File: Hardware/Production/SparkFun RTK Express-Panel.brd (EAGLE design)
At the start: 219.3 x 141.9 mm, 501 parts, among them J13 Internal, J16 External, J17 Qwiic Right Angle, J19 MICRO-SD-PUSH-PUSH-EXT-PIN, J21 USB Female Type C Connector, J24 USB Female Type C Connector, J3 USB Female Type C Connector, J32 Qwiic Right Angle, J33 Internal, J38 MICRO-SD-PUSH-PUSH-EXT-PIN, J39 External, J4 External, J40 USB Female Type C Connector, J43 USB Female Type C Connector, J5 USB Female Type C Connector, J51 Qwiic Right Angle, J52 Internal, J57 MICRO-SD-PUSH-PUSH-EXT-PIN, Q1 SIL2308-TP, Q2 MBT3904DW1T1, Q3 MBT3904DW1T1, Q4 SIL2308-TP, Q5 MBT3904DW1T1, Q6 SIL2308-TP, U1 74HC4052D, U10 MCP73833, U11 CH340C, U12 MAX17048, U13 LIS2DH12, U14 STLQ015-3.3V, U15 MCP73833, U16 74HC4052D, U17 LIS2DH12, U18 ESP-WROOM-3232D, U19 AP2112K-3.3, U2 AP2112K-3.3, U20 U-BLOX_ZED-F9P, U21 CH340C, U22 MAX17048, U23 STLQ015-3.3V, U24 MCP73833, U25 74HC4052D, U26 LIS2DH12, U27 ESP-WROOM-3232D, U3 U-BLOX_ZED-F9P, U4 STLQ015-3.3V, U5 ESP-WROOM-3232D, U6 CH340C, U7 MAX17048, U8 AP2112K-3.3, U9 U-BLOX_ZED-F9P

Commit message: LIF overlay connector, accel plane removal, full ESP32 FP.
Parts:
- removed J55: (no value), SparkFun-Connectors:1X01_NO_SILK
- removed J56: (no value), SparkFun-Connectors:FPC_12_0.5MM
- removed J57: MICRO-SD-PUSH-PUSH-EXT-PIN, SparkFun-Connectors:MICROSD-EXTERNALPIN
- added JP12: FIDUCIALUFIDUCIAL, SparkFun-Aesthetics:FIDUCIAL-MICRO
- added JP13: JUMPER-SMT_2_NO_SILK, SparkFun-Jumpers:SMT-JUMPER_2_NO_SILK
- added JP14: CONN_06, 1mm Pitch Connector:FPC_6_1MM-LIF
- J20: value (none) -> USB Female Type C Connector; device SparkFun-Connectors:FPC_12_0.5MM -> SparkFun-Connectors:USB-C-16P_4LAYER-PADS
- J21: value USB Female Type C Connector -> (none); device SparkFun-Connectors:USB-C-16P_4LAYER-PADS -> SparkFun-Connectors:JST-2-SMD
- J22: device SparkFun-Connectors:JST-2-SMD -> SparkFun-Connectors:1X02_NO_SILK
- J23: value (none) -> USB Female Type C Connector; device SparkFun-Connectors:1X02_NO_SILK -> SparkFun-Connectors:USB-C-16P_4LAYER-PADS
- J24, J43: value USB Female Type C Connector -> (none); device SparkFun-Connectors:USB-C-16P_4LAYER-PADS -> SparkFun-Connectors:JST-4-SMD-1.25MM-LOCKING
- J26, J44, J45: device SparkFun-Connectors:JST-4-SMD-1.25MM-LOCKING -> SparkFun-Connectors:1X04_NO_SILK
- J29, J47, J48: device SparkFun-Connectors:1X04_NO_SILK -> SparkFun-Connectors:1X02_NO_SILK
- J31, J49: value (none) -> Qwiic Right Angle; device SparkFun-Connectors:1X02_NO_SILK -> SparkFun-Connectors:1X04_NO_SILK
- J32: value Qwiic Right Angle -> Internal; device SparkFun-Connectors:1X04_NO_SILK -> SparkFun-Connectors:JST04_1MM_RA
- J33: value Internal -> (none); device SparkFun-Connectors:JST04_1MM_RA -> SparkFun-Connectors:1X05_NO_SILK
- J34: device SparkFun-Connectors:1X05_NO_SILK -> SparkFun-Connectors:1X04_NO_SILK
- J35: device SparkFun-Connectors:1X04_NO_SILK -> SparkFun-Connectors:1X01_NO_SILK
- J36: value (none) -> MICRO-SD-PUSH-PUSH-EXT-PIN; device SparkFun-Connectors:1X01_NO_SILK -> SparkFun-Connectors:MICROSD-EXTERNALPIN
- J37: value (none) -> External; device SparkFun-Connectors:FPC_12_0.5MM -> SparkFun-Connectors:JST04_1MM_RA
- J38: value MICRO-SD-PUSH-PUSH-EXT-PIN -> USB Female Type C Connector; device SparkFun-Connectors:MICROSD-EXTERNALPIN -> SparkFun-Connectors:USB-C-16P_4LAYER-PADS
- J39: value External -> (none); device SparkFun-Connectors:JST04_1MM_RA -> SparkFun-Connectors:JST-2-SMD
- J40: value USB Female Type C Connector -> (none); device SparkFun-Connectors:USB-C-16P_4LAYER-PADS -> SparkFun-Connectors:1X02_NO_SILK
- J41: value (none) -> USB Female Type C Connector; device SparkFun-Connectors:JST-2-SMD -> SparkFun-Connectors:USB-C-16P_4LAYER-PADS
- J42: device SparkFun-Connectors:1X02_NO_SILK -> SparkFun-Connectors:JST-4-SMD-1.25MM-LOCKING
- J50: value (none) -> Internal; device SparkFun-Connectors:1X02_NO_SILK -> SparkFun-Connectors:JST04_1MM_RA
- J51: value Qwiic Right Angle -> (none); device SparkFun-Connectors:1X04_NO_SILK -> SparkFun-Connectors:1X05_NO_SILK
- J52: value Internal -> (none); device SparkFun-Connectors:JST04_1MM_RA -> SparkFun-Connectors:1X04_NO_SILK
- J53: device SparkFun-Connectors:1X05_NO_SILK -> SparkFun-Connectors:1X01_NO_SILK
- J54: value (none) -> MICRO-SD-PUSH-PUSH-EXT-PIN; device SparkFun-Connectors:1X04_NO_SILK -> SparkFun-Connectors:MICROSD-EXTERNALPIN
- JP11, JP6: value JUMPER-SMT_2_NO_SILK -> FIDUCIALUFIDUCIAL; device SparkFun-Jumpers:SMT-JUMPER_2_NO_SILK -> SparkFun-Aesthetics:FIDUCIAL-MICRO
- JP2, JP8: value FIDUCIALUFIDUCIAL -> CONN_06; device SparkFun-Aesthetics:FIDUCIAL-MICRO -> 1mm Pitch Connector:FPC_6_1MM-LIF
- JP7: value FIDUCIALUFIDUCIAL -> JUMPER-SMT_2_NO_SILK; device SparkFun-Aesthetics:FIDUCIAL-MICRO -> SparkFun-Jumpers:SMT-JUMPER_2_NO_SILK
- R10: value 10 -> 27
- R11: value 100k -> 10
- R12: value 5.1k -> 100k
- R18: value 10k -> 5.1k; device SparkFun-Resistors:0603@1 -> SparkFun-Resistors:0603
- R45, R73: value 10k -> 1k; device SparkFun-Resistors:0603@1 -> SparkFun-Resistors:0603
- R46, R74: value 1k -> 33; device SparkFun-Resistors:0603 -> SparkFun-Resistors:1206_RA
- R50, R78: value 33 -> 100k; device SparkFun-Resistors:1206_RA -> SparkFun-Resistors:0603
- R51, R79: value 100k -> 300k
- R52, R80: value 300k -> 100k
- R53, R81: value 100k -> 10k
- R54, R82: value 10k -> 3.3k
- R55, R83: value 3.3k -> 10k
- R6: value 27 -> 10k
- moved JP7 137.9 mm to (73.9, 58.3), turned to 180 degrees
- moved R18 136.3 mm to (106.9, 10.3), flipped to the top, turned to 180 degrees
- moved JP2 125.5 mm to (51.2, 100.3), turned to 180 degrees
- moved JP3 116.5 mm to (132.1, 4.28)
- moved JP4 116.5 mm to (73.8, 105.2), flipped to the top
- moved JP5 116.5 mm to (132.1, 4.28)
- moved R6 109.3 mm to (11.2, 107.3), flipped to the bottom, turned to 0 degrees
- moved J37 105.1 mm to (171.6, 4.74), flipped to the bottom, turned to 0 degrees
- moved J42 104.0 mm to (148.7, 1.19), flipped to the top, turned to 0 degrees
- moved J20 103.9 mm to (102.9, 6.14), turned to 0 degrees
- moved J41 102.1 mm to (183.0, 6.14), turned to 0 degrees
- moved J23 101.4 mm to (114.3, 6.14), flipped to the top, turned to 0 degrees
- moved J39 100.5 mm to (151.6, 103.3), flipped to the top, turned to 90 degrees
- moved J40 99.3 mm to (158.9, 104.7), flipped to the bottom, turned to 270 degrees
- moved J21 99.2 mm to (82.9, 103.3), turned to 90 degrees
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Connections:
- net 3.3V1: now also J25.1, J27.4, J31.2, J36.4, R12.2, R55.2; no longer J26.1, J29.4, J33.2, J38.4, R11.2, R56.2
- net 3.3V2: now also J37.2, J43.1, J45.4, J46.4, J49.2, J50.2, J54.4, R83.2; no longer J39.2, J45.1, J47.4, J48.4, J51.2, J52.2, J57.4, R84.2
- net ANT_VCC1: now also R11.1; no longer R10.1
- net CC10: now also J38.B5; no longer J40.B5
- net CC11: now also J41.B5; no longer J43.B5
- net CC12: now also J41.A5; no longer J43.A5
- net CC5: now also J20.A5; no longer J21.A5
- net CC6: now also J20.B5, R18.2; no longer J21.B5, R12.2
- net CC7: now also J23.B5; no longer J24.B5
- net CC8: now also J23.A5; no longer J24.A5
- net CC9: now also J38.A5; no longer J40.A5
- net CHG_LED_RES: now also JP2.2; no longer J20.3, J20.4
- net CHG_LED_RES1: now also J34.2, JP8.2; no longer J35.2, J37.3, J37.4
- net CHG_LED_RES2: now also J52.2, JP14.2; no longer J54.2, J56.3, J56.4
- net CHG_THERM1: now also R6.2; no longer R18.2
- net CHG_THERM2: now also R56.2; no longer R45.2
- net CHG_THERM3: now also R84.2; no longer R73.2
- net D+2: now also R8.1; no longer R6.1
- net D-2: now also R10.1; no longer R8.1
- net ESP32_EN1: now also J30.1; no longer J31.1
- net ESP32_EN2: now also J48.1; no longer J50.1
- net ESP_13/POWER_CTRL1: now also R50.1, R51.2; no longer R51.1, R52.2
- net ESP_13/POWER_CTRL2: now also R78.1, R79.2; no longer R79.1, R80.2
- net ESP_14/SETUP_BUTTON: now also JP2.4; no longer J20.7, J20.8
- net ESP_14/SETUP_BUTTON1: now also J34.3, JP8.4; no longer J35.3, J37.7, J37.8
- net ESP_14/SETUP_BUTTON2: now also J52.3, JP14.4; no longer J54.3, J56.7, J56.8
- net ESP_18/SCK1: now also J36.5; no longer J38.5
- net ESP_18/SCK2: now also J54.5; no longer J57.5
- net ESP_19/CIPO1: now also J36.7; no longer J38.7
- net ESP_19/CIPO2: now also J54.7; no longer J57.7
- net ESP_21/SDA1: now also J31.3, R47.P7; no longer J33.3, R48.P7
- net ESP_21/SDA2: now also J37.3, J49.3, J50.3, R75.P7; no longer J39.3, J51.3, J52.3, R76.P7
- net ESP_22/SCL1: now also J31.4, R47.P8; no longer J33.4, R48.P8
- net ESP_22/SCL2: now also J37.4, J49.4, J50.4, R75.P8; no longer J39.4, J51.4, J52.4, R76.P8
- net ESP_23/COPI1: now also J36.3; no longer J38.3
- net ESP_23/COPI2: now also J54.3; no longer J57.3
- net ESP_25/SD_!CS!1: now also J36.2; no longer J38.2
- net ESP_25/SD_!CS!2: now also J54.2; no longer J57.2
- net ESP_26/ZED_TX_READY_LV1: now also R48.P4; no longer R49.P4
- net ESP_26/ZED_TX_READY_LV2: now also R76.P4; no longer R77.P4
- net ESP_27/FAST_OFF1: now also R51.1; no longer R52.1
- net ESP_27/FAST_OFF2: now also R79.1; no longer R80.1
- net ESP_4/ACCEL_INT1: now also J35.1, JP7.1; no longer J36.1, JP6.1
- net ESP_4/ACCEL_INT2: now also J53.1, JP13.1; no longer J55.1, JP11.1
- net ESP_D1+1: now also J23.A6, J23.B6; no longer J24.A6, J24.B6
- net ESP_D1+2: now also J41.A6, J41.B6; no longer J43.A6, J43.B6
- net ESP_D1-1: now also J23.A7, J23.B7; no longer J24.A7, J24.B7
- net ESP_D1-2: now also J41.A7, J41.B7; no longer J43.A7, J43.B7
- net ESP_I16/ZED-TXO2: now also J29.1, R47.P5; no longer J30.1, R48.P5
- net ESP_I16/ZED-TXO3: now also J47.1, R75.P5; no longer J49.1, R76.P5
- net ESP_I34/ZED_TX_READY1: now also J33.1, R48.P5; no longer J34.1, R49.P5
- net ESP_I34/ZED_TX_READY2: now also J51.1, R76.P5; no longer J53.1, R77.P5
- net ESP_I35/DEVICE_SENSE1: now also R54.2, R55.1; no longer R55.2, R56.1
- net ESP_I35/DEVICE_SENSE2: now also R82.2, R83.1; no longer R83.2, R84.1
- net ESP_O17/ZED-RXI2: now also J29.2, R45.2, R47.P6; no longer J30.2, R46.2, R48.P6
- net ESP_O17/ZED-RXI3: now also J47.2, R73.2, R75.P6; no longer J49.2, R74.2, R76.P6
- net EXTERNAL_DATA_IN1: now also J25.3, J27.2; no longer J26.3, J28.2
- net EXTERNAL_DATA_IN2: now also J43.3, J45.2; no longer J45.3, J47.2
- net EXTERNAL_DATA_OUT1: now also J25.2, J27.3; no longer J26.2, J28.3
- net EXTERNAL_DATA_OUT2: now also J43.2, J45.3; no longer J45.2, J47.3
- net EXTINT_LV1: now also R49.P2; no longer R50.P2
- net EXTINT_LV2: now also R77.P2; no longer R78.P2
- net FENCE_LV1: now also R46.P4; no longer R47.P4
- net FENCE_LV2: now also R74.P4; no longer R75.P4
- net GND: now also JP2.6, R6.1; no longer J20.11, J20.12, R18.1
- net GND1: now also J20.GND, J20.GND2, J20.SHLD1, J20.SHLD2, J20.SHLD3, J20.SHLD4, J21.1, J22.2, J23.GND, J23.GND2, J23.SHLD1, J23.SHLD2, J23.SHLD3, J23.SHLD4, J24.4, J26.1, J30.2, J31.1, J34.1, J36.10, J36.11, J36.12, J36.13, J36.6, J36.9, JP8.6, R18.1, R54.1, R56.1; no longer J21.GND, J21.GND2, J21.SHLD1, J21.SHLD2, J21.SHLD3, J21.SHLD4, J22.1, J23.2, J24.GND, J24.GND2, J24.SHLD1, J24.SHLD2, J24.SHLD3, J24.SHLD4, J26.4, J29.1, J31.2, J33.1, J35.1, J37.11, J37.12, J38.10, J38.11, J38.12, J38.13, J38.6, J38.9, R11.1, R45.1, R55.1
- net GND2: now also J37.1, J38.GND, J38.GND2, J38.SHLD1, J38.SHLD2, J38.SHLD3, J38.SHLD4, J40.2, J41.GND, J41.GND2, J41.SHLD1, J41.SHLD2, J41.SHLD3, J41.SHLD4, J42.4, J43.4, J44.1, J45.1, J48.2, J49.1, J50.1, J54.10, J54.11, J54.12, J54.13, J54.6, J54.9, JP14.6, R82.1, R84.1; no longer J40.GND, J40.GND2, J40.SHLD1, J40.SHLD2, J40.SHLD3, J40.SHLD4, J41.1, J42.2, J43.GND, J43.GND2, J43.SHLD1, J43.SHLD2, J43.SHLD3, J43.SHLD4, J44.4, J45.4, J47.1, J48.1, J50.2, J51.1, J54.1, J56.11, J56.12, J57.10, J57.11, J57.12, J57.13, J57.6, J57.9, R73.1, R83.1
- net LIPO_RAW1: now also J21.2; no longer J22.2
- net LIPO_RAW2: now also J39.2; no longer J41.2
- net N$10: now also J23.VBUS1, J23.VBUS2; no longer J24.VBUS1, J24.VBUS2
- net N$14: now also J20.VBUS1, J20.VBUS2; no longer J21.VBUS1, J21.VBUS2
- net N$17: now also R45.1; no longer R46.1
- net N$18: now also R52.1; no longer R53.1
- net N$2: now also R8.2; no longer R6.2
- net N$27: now also J41.VBUS1, J41.VBUS2; no longer J43.VBUS1, J43.VBUS2
- net N$28: now also J38.VBUS1, J38.VBUS2; no longer J40.VBUS1, J40.VBUS2
- net N$3: now also R10.2; no longer R8.2
- net N$30: now also R73.1; no longer R74.1
- net N$31: now also R80.1; no longer R81.1
- net N$7: now also R11.2; no longer R10.2
- net POWER_BTN: now also JP2.5; no longer J20.10, J20.9
- net POWER_BTN1: now also J34.4, JP7.2, JP8.5, R53.1; no longer J35.4, J37.10, J37.9, JP6.2, R54.1
- net POWER_BTN2: now also J52.4, JP13.2, JP14.5, R81.1; no longer J54.4, J56.10, J56.9, JP11.2, R82.1
- net PPS1: now also R49.P1; no longer R50.P1
- net PPS2: now also R77.P1; no longer R78.P1
- net RTK_LV1: now also R46.P3; no longer R47.P3
- net RTK_LV2: now also R74.P3; no longer R75.P3
- net RX2_LV1: now also R46.P2; no longer R47.P2
- net RX2_LV2: now also R74.P2; no longer R75.P2
- net RXLV1: now also R47.P3; no longer R48.P3
- net RXLV2: now also R75.P3; no longer R76.P3
- net SCL_LV1: now also R47.P1; no longer R48.P1
- net SCL_LV2: now also R75.P1; no longer R76.P1
- net SDA_LV1: now also R47.P2; no longer R48.P2
- net SDA_LV2: now also R75.P2; no longer R76.P2
- net TX2_LV1: now also R46.P1; no longer R47.P1
- net TX2_LV2: now also R74.P1; no longer R75.P1
- net TXLV1: now also R47.P4; no longer R48.P4
- net TXLV2: now also R75.P4; no longer R76.P4
- net UNP_D+1: now also J20.A6, J20.B6; no longer J21.A6, J21.B6
- net UNP_D+2: now also J38.A6, J38.B6; no longer J40.A6, J40.B6
- net UNP_D-1: now also J20.A7, J20.B7; no longer J21.A7, J21.B7
- net UNP_D-2: now also J38.A7, J38.B7; no longer J40.A7, J40.B7
- net VOUT1: now also J24.1, J26.4, R50.2; no longer J25.1, J27.4, R51.2
- net VOUT2: now also J42.1, J44.4, R78.2; no longer J44.1, J46.4, R79.2
- net V_BATT1: now also J22.1; no longer J23.1
- net V_BATT2: now also J40.1; no longer J42.1
- net V_RAW1: now also R52.2; no longer R54.2
- net V_RAW2: now also R80.2; no longer R82.2
- net V_USB: now also JP2.1; no longer J20.1, J20.2
- net V_USB1: now also JP8.1; no longer J37.1, J37.2
- net V_USB2: now also JP14.1; no longer J56.1, J56.2
- net ZED-RXI1: now also J24.3, J26.2, R46.P7; no longer J25.3, J27.2, R47.P7
- net ZED-RXI3: now also J42.3, J44.2, R74.P7; no longer J44.3, J46.2, R75.P7
- net ZED-TXO1: now also J24.2, J26.3, R46.P8; no longer J25.2, J27.3, R47.P8
- net ZED-TXO3: now also J42.2, J44.3, R74.P8; no longer J44.2, J46.3, R75.P8
- net ZED_!RESET!1: now also J33.3, R48.P7; no longer J34.3, R49.P7
- net ZED_!RESET!2: now also J51.3, R76.P7; no longer J53.3, R77.P7
- net ZED_!RESET!_LV1: now also R48.P2; no longer R49.P2
- net ZED_!RESET!_LV2: now also R76.P2; no longer R77.P2
- net ZED_!SAFE!1: now also J33.4, R48.P8; no longer J34.4, R49.P8
- net ZED_!SAFE!2: now also J51.4, R76.P8; no longer J53.4, R77.P8
- net ZED_!SAFE!_LV1: now also R48.P1; no longer R49.P1
- net ZED_!SAFE!_LV2: now also R76.P1; no longer R77.P1
- net ZED_D_SEL1: now also J33.2, R48.P6; no longer J34.2, R49.P6
- net ZED_D_SEL2: now also J51.2, R76.P6; no longer J53.2, R77.P6
- net ZED_D_SEL_LV1: now also R48.P3; no longer R49.P3
- net ZED_D_SEL_LV2: now also R76.P3; no longer R77.P3
- net ZED_EXTINT1: now also R49.P7; no longer R50.P7
- net ZED_EXTINT2: now also R77.P7; no longer R78.P7
- net ZED_FENCE_STAT1: now also J28.2, R46.P5; no longer J29.2, R47.P5
- net ZED_FENCE_STAT2: now also J46.2, R74.P5; no longer J48.2, R75.P5
- net ZED_PPS_STAT1: now also J33.5, R49.P8; no longer J34.5, R50.P8
- net ZED_PPS_STAT2: now also J51.5, R77.P8; no longer J53.5, R78.P8
- net ZED_RTK_STAT1: now also J28.3, R46.P6; no longer J29.3, R47.P6
- net ZED_RTK_STAT2: now also J46.3, R74.P6; no longer J48.3, R75.P6
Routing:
- net CHG_LED_RES: track 26.4 -> 22.7 mm
- net CHG_LED_RES2: track 26.4 -> 22.7 mm
- net CHG_LED_RES1: track 26.4 -> 22.7 mm
- net ESP32_EN2: track 76.0 -> 78.2 mm
- net ESP32_EN: track 76.0 -> 78.2 mm
- net ESP32_EN1: track 76.0 -> 78.2 mm
- net ESP_14/SETUP_BUTTON2: track 31.0 -> 31.7 mm
- net ESP_14/SETUP_BUTTON1: track 31.0 -> 31.7 mm
- net ESP_14/SETUP_BUTTON: track 31.0 -> 31.7 mm
- net POWER_BTN: track 143.0 -> 143.6 mm
- net POWER_BTN2: track 143.0 -> 143.6 mm
- net POWER_BTN1: track 143.0 -> 143.6 mm
- net V_USB2: track 189.7 -> 190.2 mm
- net V_USB1: track 189.7 -> 190.2 mm
- net V_USB: track 189.7 -> 190.2 mm

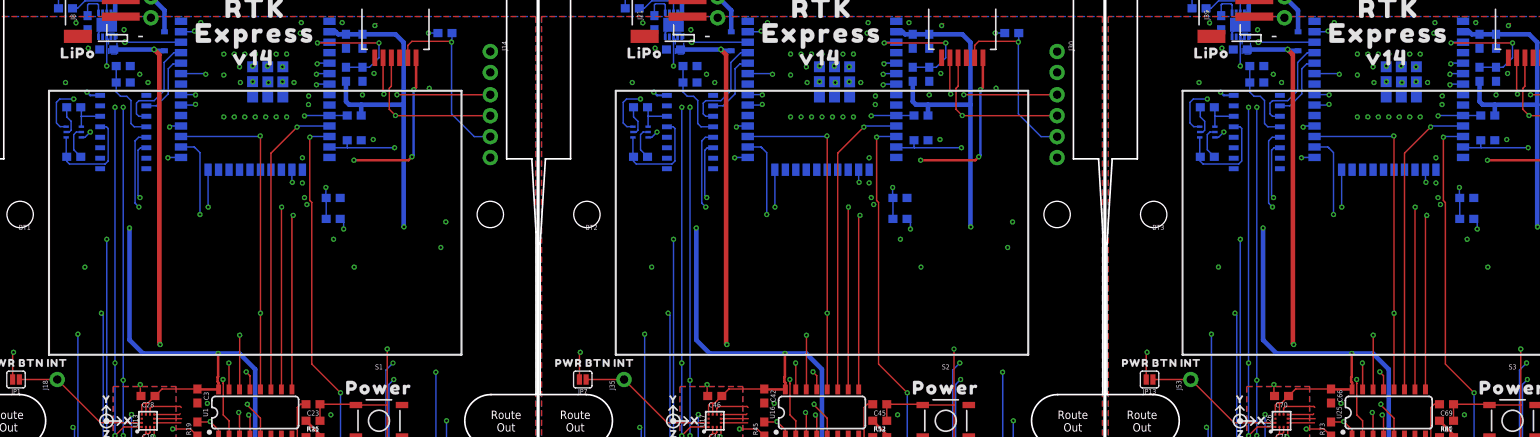
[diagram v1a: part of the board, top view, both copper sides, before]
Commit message: v15. Fix tCream on LIF connector. Correct CH340 3.3V.
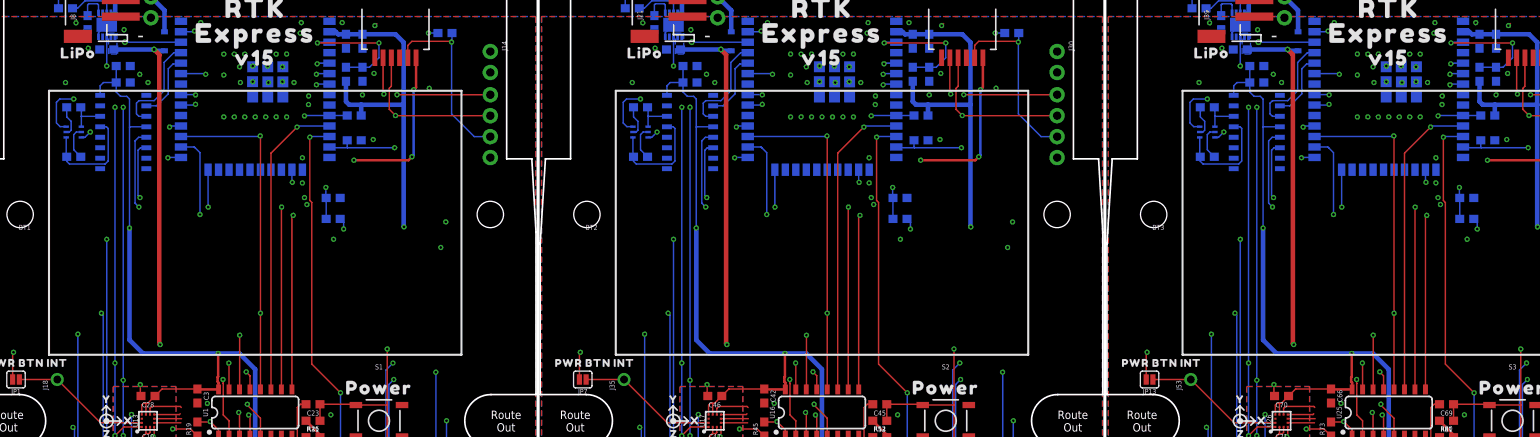
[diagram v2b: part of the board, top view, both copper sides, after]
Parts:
- J19, J36, J54: value MICRO-SD-PUSH-PUSH-EXT-PIN -> MICROSD
- JP14, JP2, JP8: value CONN_06 -> (none); device 1mm Pitch Connector:FPC_6_1MM-LIF -> SparkFun-Connectors:FPC_6_1MM-LIF
- MEAS, MEAS1, MEAS2, MEAS3, MEAS4, MEAS5: value JUMPER-COMBO_2_NC_TRACE -> (none)
- U$12: device output:V140 -> output:#3V3#0
- U$124, U$186: device output:V140 -> output:V150
- U$18: device output:#3V3#0 -> output:V150
- moved U$12 110.1 mm to (122.4, 31.7)
- moved U$18 110.0 mm to (34.2, 97.3)
- moved U$124 0.20 mm to (102.9, 97.3)
- moved U$186 0.20 mm to (171.6, 97.3)
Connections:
- removed net N$1 (its old number): C13.1, C14.1, U6.4
- removed net N$19 (its old number): C36.1, C37.1, U11.4
- removed net N$33: C60.1, C61.1, U21.4
- net 3.3V: now also C13.1, C14.1, U6.16, U6.4
- net 3.3V1: now also C36.1, C37.1, U11.16, U11.4
- net 3.3V2: now also C60.1, C61.1, U21.16, U21.4
- net V_USB: no longer U6.16
- net V_USB1: no longer U11.16
- net V_USB2: no longer U21.16
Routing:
- net V_USB2: track 190.2 -> 134.5 mm, vias 12 -> 9
- net V_USB1: track 190.2 -> 134.5 mm, vias 12 -> 9
- net V_USB: track 190.2 -> 134.5 mm, vias 12 -> 9
- net 3.3V1: track 308.1 -> 334.2 mm
- net 3.3V: track 308.1 -> 334.2 mm
- net 3.3V2: track 308.1 -> 334.2 mm
- net N$19 (its old number): track 10.2 -> 0.00 mm
- net N$33: track 10.2 -> 0.00 mm
- net N$1 (its old number): track 10.2 -> 0.00 mm
- net ESP_I39/ADC39: track 60.8 -> 58.6 mm
- net ESP_I39/ADC2: track 60.8 -> 58.6 mm
- net ESP_I39/ADC1: track 60.8 -> 58.6 mm
- net ESP_I34/ZED_TX_READY2: track 103.0 -> 100.7 mm
- net ESP_I34/ZED_TX_READY1: track 103.0 -> 100.7 mm
- net ESP_I34/ZED_TX_READY: track 103.0 -> 100.7 mm

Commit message: Production files for v15
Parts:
- moved JP14 2.00 mm to (188.6, 98.3)
- moved JP2 2.00 mm to (51.2, 98.3)
- moved JP8 2.00 mm to (119.9, 98.3)
- moved U$120 2.00 mm to (119.9, 103.3)
- moved U$182 2.00 mm to (188.6, 103.3)
- moved U$8 2.00 mm to (51.2, 103.3)
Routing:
- net V_USB2: track 134.5 -> 132.5 mm
- net V_USB1: track 134.5 -> 132.5 mm
- net V_USB: track 134.5 -> 132.5 mm
- net POWER_BTN2: track 143.6 -> 141.6 mm
- net POWER_BTN1: track 143.6 -> 141.6 mm
- net POWER_BTN: track 143.6 -> 141.6 mm
- net ESP_14/SETUP_BUTTON2: track 31.7 -> 29.7 mm
- net ESP_14/SETUP_BUTTON1: track 31.7 -> 29.7 mm
- net ESP_14/SETUP_BUTTON: track 31.7 -> 29.7 mm
- net CHG_LED_RES2: track 22.7 -> 24.7 mm
- net CHG_LED_RES1: track 22.7 -> 24.7 mm
- net CHG_LED_RES: track 22.7 -> 24.7 mm
